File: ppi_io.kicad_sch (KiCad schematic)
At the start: 7 parts

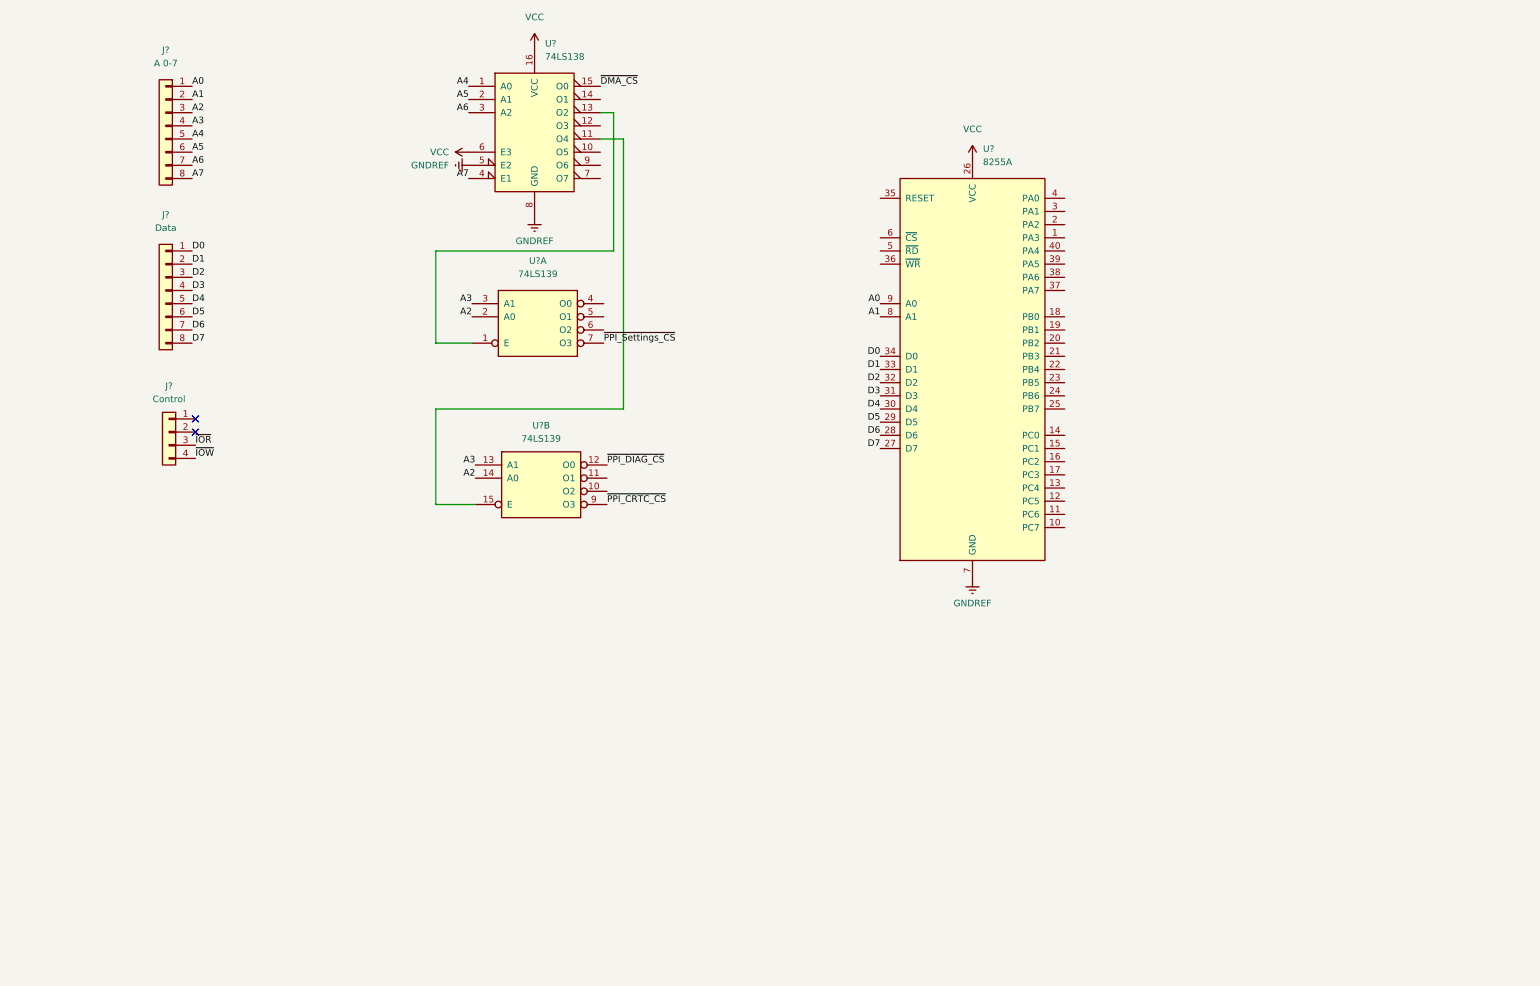
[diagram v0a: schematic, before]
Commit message: Updated to version 8
Changed to version 8; added 96-pin connectors; described ports at PPI_Settings
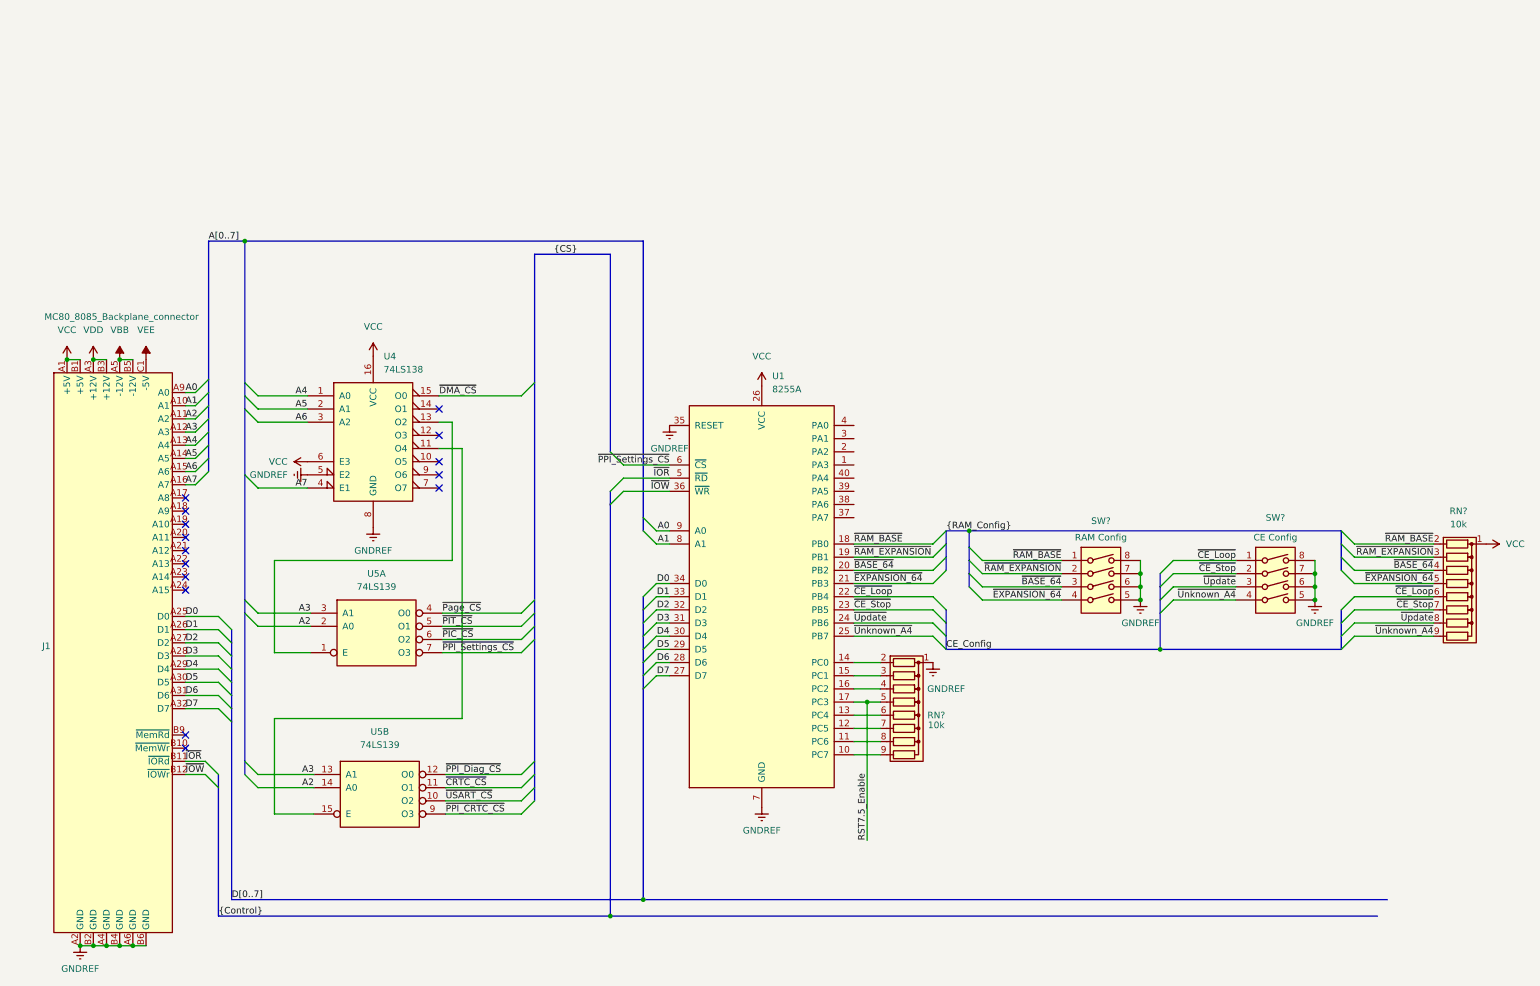
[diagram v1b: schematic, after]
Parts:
- removed J?: Data, symbol Connector_Generic:Conn_01x08
- removed J?: Control, symbol Connector_Generic:Conn_01x04
- removed J?: A 0-7, symbol Connector_Generic:Conn_01x08
- added J1: MC80_8085_Backplane_connector, symbol connector-miscellaneous:MC80_8085_Backplane_connector
- added RN? (x2): 10k, Resistor_THT:R_Array_SIP9, symbol Device:R_Network08
- added SW?: CE Config, symbol Switch:SW_DIP_x04
- added SW?: RAM Config, symbol Switch:SW_DIP_x04
- gave numbers to parts that had none: 3
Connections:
- net A0: now also J1.A9 (A0)
- net A1: now also J1.A10 (A1)
- net A2: now also J1.A11 (A2)
- net A3: now also J1.A12 (A3)
- net A4: now also J1.A13 (A4)
- net A5: now also J1.A14 (A5)
- net A6: now also J1.A15 (A6)
- net A7: now also J1.A16 (A7)
- net D0: now also J1.A25 (D0)
- net D1: now also J1.A26 (D1)
- net D2: now also J1.A27 (D2)
- net D3: now also J1.A28 (D3)
- net D4: now also J1.A29 (D4)
- net D5: now also J1.A30 (D5)
- net D6: now also J1.A31 (D6)
- net D7: now also J1.A32 (D7)
- net GNDREF: now also U1.35 (RESET), J1.A2 (GND), J1.A4 (GND), J1.A6 (GND), J1.B2 (GND), J1.B4 (GND), J1.B6 (GND), RN?.1 (common), SW?.5, SW?.5, SW?.6, SW?.6, SW?.7, SW?.7, SW?.8, SW?.8
- net VCC: now also J1.A1 (+5V), J1.B1 (+5V), RN?.1 (common)
- net ~{IOR}: now also U1.5 (~{RD}), J1.B11 (~{IORd})
- net ~{IOW}: now also U1.36 (~{WR}), J1.B12 (~{IOWr})
- net ~{PPI_Settings_CS}: now also U1.6 (~{CS})
- net ~{USART_CS}: now reaches U5.10 (O2)
- net ~{CRTC_CS}: now reaches U5.11 (O1)
- net ~{Page_CS}: now reaches U5.4 (O0)
- net ~{PIT_CS}: now reaches U5.5 (O1)
- net ~{PIC_CS}: now reaches U5.6 (O2)
- net at U1.10 (PC7): now also RN?.9 (R8)
- net at U1.11 (PC6): now also RN?.8 (R7)
- net at U1.12 (PC5): now also RN?.7 (R6)
- net at U1.13 (PC4): now also RN?.6 (R5)
- net at U1.14 (PC0): now also RN?.2 (R1)
- net at U1.15 (PC1): now also RN?.3 (R2)
- net at U1.16 (PC2): now also RN?.4 (R3)
- net RST7.5_Enable: now reaches U1.17 (PC3)
- net RST7.5_Enable: now also RN?.5 (R4)
- net ~{RAM_BASE}: now reaches U1.18 (PB0)
- net ~{RAM_BASE}: now also RN?.2 (R1), SW?.1
- net ~{RAM_EXPANSION}: now reaches U1.19 (PB1)
- net ~{RAM_EXPANSION}: now also RN?.3 (R2), SW?.2
- net ~{BASE_64}: now reaches U1.20 (PB2)
- net ~{BASE_64}: now also RN?.4 (R3), SW?.3
- net ~{EXPANSION_64}: now reaches U1.21 (PB3)
- net ~{EXPANSION_64}: now also RN?.5 (R4), SW?.4
- net ~{CE_Loop}: now reaches U1.22 (PB4)
- net ~{CE_Loop}: now also RN?.6 (R5), SW?.1
- net ~{CE_Stop}: now reaches U1.23 (PB5)
- net ~{CE_Stop}: now also RN?.7 (R6), SW?.2
- net ~{Update}: now reaches U1.24 (PB6)
- net ~{Update}: now also RN?.8 (R7), SW?.3
- net ~{Unknown_A4}: now reaches U1.25 (PB7)
- net ~{Unknown_A4}: now also RN?.9 (R8), SW?.4
- net ~{PPI_DIAG_CS} renamed ~{PPI_Diag_CS}
- new net VBB: J1.A5 (-12V), J1.B5 (-12V)
- new net VDD: J1.A3 (+12V), J1.B3 (+12V)
- new net VEE: J1.C1 (-5V)
- no-connect marks 2 -> 15
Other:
- moved on the sheet: U1, U4, U5A, U5B
